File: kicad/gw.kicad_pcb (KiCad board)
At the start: 2 copper layers, 20 parts, among them IC1 ATMEGA8A-A, P1 12v-gnd-clunet, P2 CONN_01X08, P3 CONN_RST, P9 CON_RPI_1-10, Q1 BC858, U1 MC78L05ACD

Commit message: Добавлено кое-что
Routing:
- removed copper zone on F.Cu, net GND
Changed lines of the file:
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@@
     (links 45)
     (no_connects 1)
-    (area 68.047618 31.5 148.352383 57.5)
+    (area 68.047618 31.875 148.352383 56.765)
     (thickness 1.6)
-    (drawings 10)
+    (drawings 7)
     (tracks 240)
     (zones 0)
@@
     )
   )
-  (target plus (at 136 55) (size 5) (width 0.15) (layer Edge.Cuts))
-  (target plus (at 136 34) (size 5) (width 0.15) (layer Edge.Cuts))
-  (target plus (at 81 55) (size 5) (width 0.15) (layer Edge.Cuts))
   (gr_line (start 136 34.6) (end 136 55.2) (angle 90) (layer Dwgs.User) (width 0.2))
   (gr_line (start 81 34.6) (end 136 34.6) (angle 90) (layer Dwgs.User) (width 0.2))
@@
   (segment (start 104.6 36) (end 107.75 36) (width 0.4) (layer F.Cu) (net 36))
   (segment (start 107.6 35.85) (end 107.75 36) (width 0.4) (layer F.Cu) (net 36))
-  (zone (net 2) (net_name GND) (layer F.Cu) (hatch edge 0.508)
-    (connect_pads (clearance 0.508))
-    (min_thickness 0.254)
-    (fill yes (arc_segments 16) (thermal_gap 0.508) (thermal_bridge_width 0.508))
-    (polygon
-      (pts
-        (xy 136 55) (xy 81 55) (xy 81 35) (xy 136 35)
-      )
-    )
-  )
 )

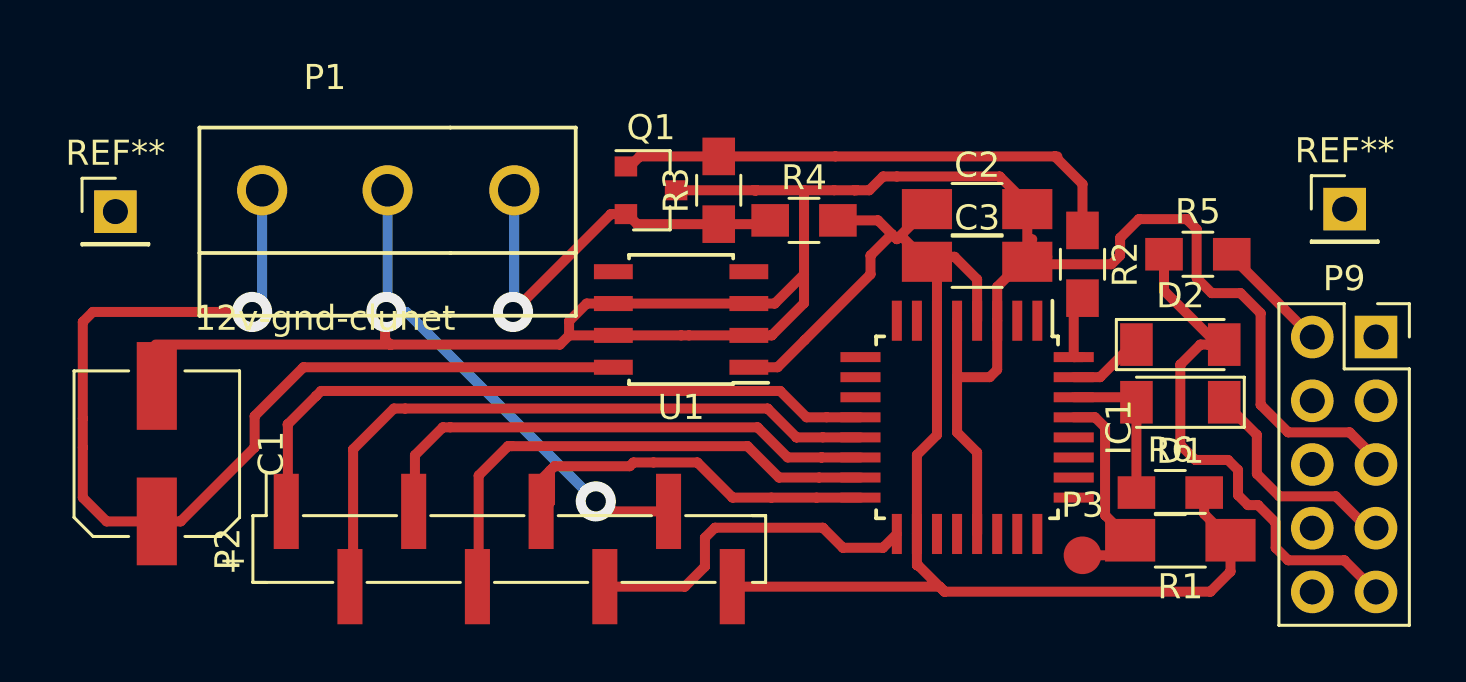
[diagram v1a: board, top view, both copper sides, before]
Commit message: Заменение схемы. Ве-таки с одной ногой работает не очень хорошо (полой низкий уровень) Добавлен дополнительный транзистор для запирания утечки.
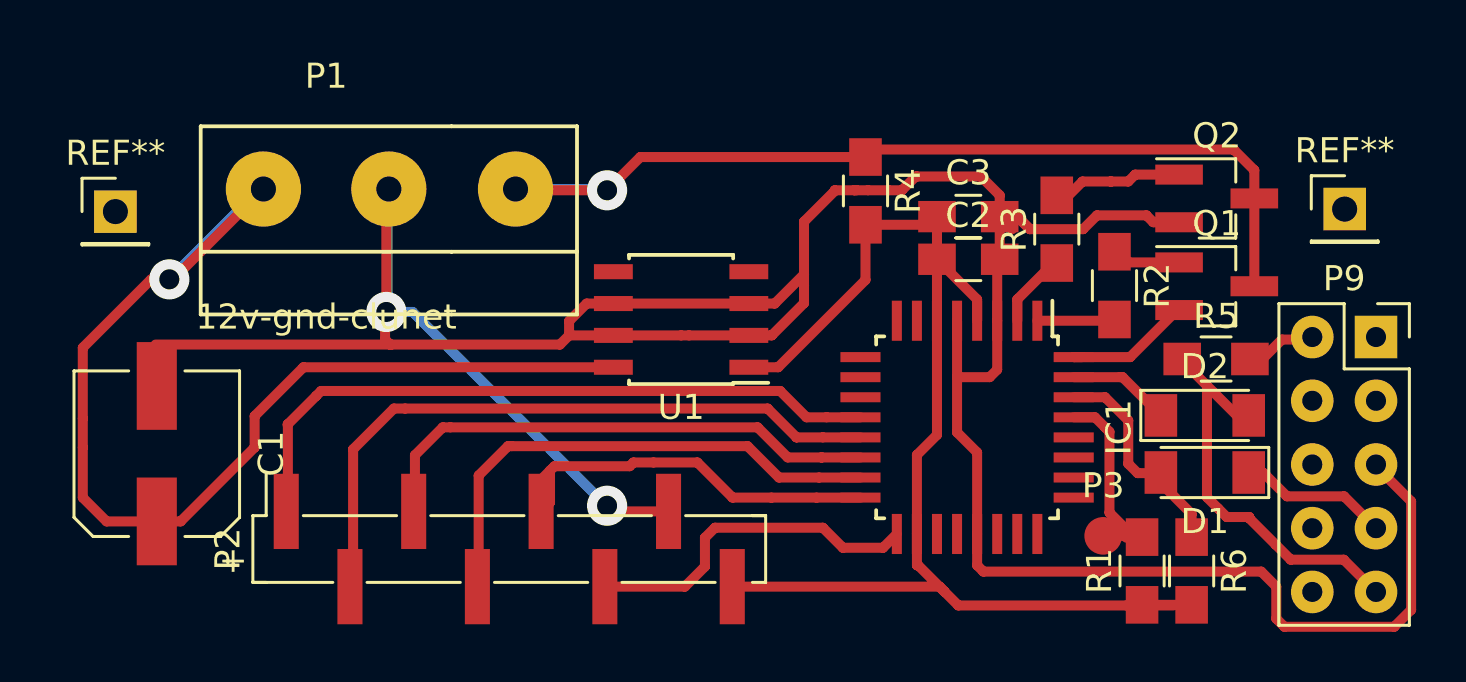
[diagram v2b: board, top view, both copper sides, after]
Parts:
- added Q2: BC847, TO_SOT_Packages_SMD:SOT-23_Handsoldering, F.Cu at (127.6, 37.7)
- C2, C3: footprint Capacitors_SMD:C_1206_HandSoldering -> Capacitors_SMD:C_0805_HandSoldering
- Q1: value BC858 -> BC847; footprint TO_SOT_Packages_SMD:SOT-23 -> TO_SOT_Packages_SMD:SOT-23_Handsoldering
- R1: footprint Resistors_SMD:R_1206_HandSoldering -> Resistors_SMD:R_0805_HandSoldering
- R3: value 22K -> 2.2K
- moved Q1 22.9 mm to (127.6, 41.2)
- moved R3 13.6 mm to (121.2, 38.9)
- moved R5 4.24 mm to (127.6, 44.1)
- moved R6 3.24 mm to (126.6, 52.5), turned to 270 degrees
- moved D2 2.99 mm to (127.1, 46.3)
- moved D1 2.96 mm to (127.1, 48.6)
- moved R4 2.72 mm to (113.6, 37.4), turned to 270 degrees
- moved C2 2.03 mm to (117.7, 40.1)
- moved R1 1.96 mm to (124.6, 52.5), turned to 90 degrees
- moved C3 1.83 mm to (117.7, 38.4)
- moved R2 1.53 mm to (123.5, 41.1)
- moved P3 1.13 mm to (123.1, 51.1)
- moved P1 0.07 mm to (92.1, 37.3)
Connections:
- net /PC5 renamed Net-(IC1-Pad28)
- IC1 pad 2: /PD4 -> Net-(IC1-Pad2)
- Q1 pad 2: /clunet -> Net-(IC1-Pad32)
- Q1 pad 3: GND -> /clunet
- R2 pad 2: Net-(IC1-Pad32) -> /PD3
- R3 pad 1: /clunet -> Net-(IC1-Pad2)
- R3 pad 2: Net-(Q1-Pad1) -> Net-(Q2-Pad1)
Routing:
- net /clunet: track 16.5 -> 38.8 mm
- net Net-(Q1-Pad1): track 21.0 -> 2.83 mm
- net GND: track 120.0 -> 129.2 mm
- net +5V: track 57.5 -> 50.5 mm
- net Net-(Q2-Pad1): track 0.00 -> 5.51 mm
- net /rpi_rx: track 22.2 -> 16.9 mm
- net /rpi_tx: track 9.95 -> 6.79 mm
- net /PD3: track 0.00 -> 3.02 mm
- net Net-(IC1-Pad2): track 0.00 -> 2.76 mm
- net /mc_rx: track 6.18 -> 8.68 mm
- net Net-(IC1-Pad32): track 2.89 -> 5.38 mm
- net +12V: track 43.8 -> 45.9 mm
- net +3V3: track 4.63 -> 3.15 mm
- net /mc_tx: track 3.04 -> 4.11 mm

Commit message: ЧТо-то еще поменялось
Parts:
- moved IC1 64.0 mm to (55.4, 32.0)
- moved P2 64.0 mm to (37.1, 36.9)
- moved R2 64.0 mm to (61.3, 26.4)
- moved C2 64.0 mm to (55.5, 25.4)
- moved C3 64.0 mm to (55.5, 23.6)
- moved D1 64.0 mm to (64.9, 33.9)
- moved D2 64.0 mm to (64.9, 31.6)
- moved P3 64.0 mm to (60.8, 36.4)
- moved Q1 64.0 mm to (65.3, 26.4)
- moved Q2 64.0 mm to (65.3, 22.9)
- moved R1 64.0 mm to (62.4, 37.8)
- moved R5 64.0 mm to (65.3, 29.3)
- moved R6 64.0 mm to (64.3, 37.8)
- moved REF** 64.0 mm to (21.4, 23.4)
- moved U1 64.0 mm to (44.0, 27.8)
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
